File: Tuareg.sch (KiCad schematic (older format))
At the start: 1 part, among them CON1 ModICE_48

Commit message: changed to discrete crank vr sensor cirquitry
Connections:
- net con_vrspare+: no longer names the net of CON1.37 (D24)
- net con_vrspare-: no longer names the net of CON1.36 (D23)
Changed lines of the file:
@@
-$EndSheet
-$Sheet
-S 4300 6600 1800 950
-U 5BCA424F
-F0 "engine position sensors" 50
-F1 "engine_pos.sch" 50
-F2 "crank_signal" O R 6100 6800 50
-F3 "vr_spare" O R 6100 7150 50
-F4 "vr_crank+" I L 4300 6800 50
-F5 "vr_crank-" I L 4300 6950 50
-F6 "vr_spare-" I L 4300 7350 50
-F7 "vr_spare+" I L 4300 7150 50
 $EndSheet
 $Sheet
@@
 ach8
 Wire Wire Line
-	6100 7150 7450 7150
-Text Label 6400 7150 0    50   ~ 0
-vr_spare
-Wire Wire Line
 	6100 5400 7450 5400
 Wire Wire Line
@@
 	3450 6950 4300 6950
 Wire Wire Line
-	3450 7150 4300 7150
-Wire Wire Line
-	3450 7350 4300 7350
-Wire Wire Line
 	3450 7950 4300 7950
 Wire Wire Line
@@
 Text Label 3450 6950 0    50   ~ 0
 con_vrcrank-
-Text Label 3450 7150 0    50   ~ 0
-con_vrspare+
-Text Label 3450 7350 0    50   ~ 0
-con_vrspare-
 Text Label 3450 7950 0    50   ~ 0
 con_knock1
@@
 	20150 6650 20400 6650
 Wire Wire Line
-	20150 7150 20400 7150
-Wire Wire Line
 	20150 7250 20400 7250
 Text Label 20400 7750 0    50   ~ 0
@@
 Wire Wire Line
 	20400 7750 20150 7750
-Text Label 20400 7150 0    50   ~ 0
-con_vrspare+
-Text Label 20400 7050 0    50   ~ 0
-con_vrspare-
 Text Label 20400 6850 0    50   ~ 0
 con_vrcrank-
@@
 Wire Wire Line
 	20400 6850 20150 6850
-Wire Wire Line
-	20400 7050 20150 7050
 Wire Wire Line
 	20400 7350 20150 7350
@@
 Wire Wire Line
 	3450 4750 4300 4750
+$Sheet
+S 4300 6600 1800 950
+U 5BCA424F
+F0 "engine position sensors" 50
+F1 "engine_pos.sch" 50
+F2 "crank_signal" O R 6100 6800 50
+F3 "vr_crank+" I L 4300 6800 50
+F4 "vr_crank-" I L 4300 6950 50
+$EndSheet
 $EndSCHEMATC

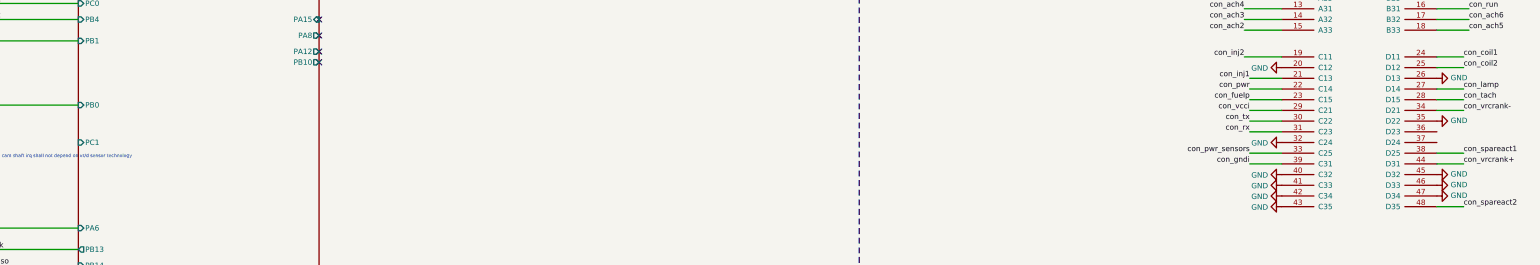
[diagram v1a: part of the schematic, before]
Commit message: migration to kicad 5.1.2
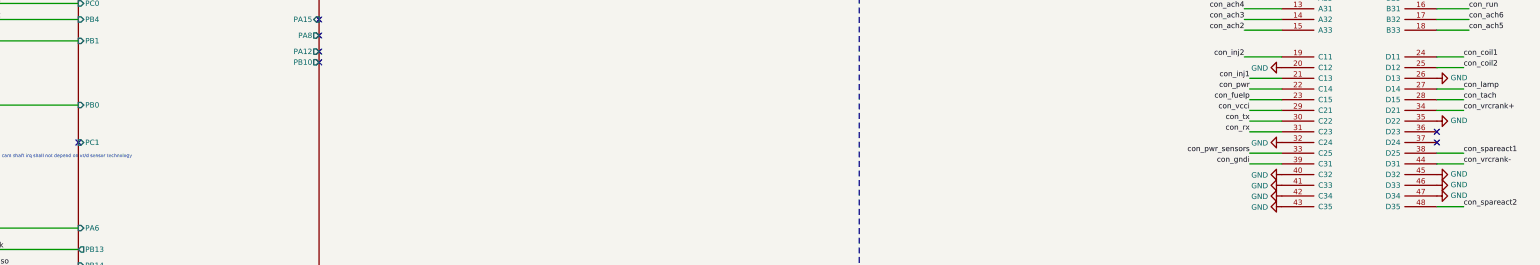
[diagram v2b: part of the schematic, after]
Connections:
- net con_vrcrank+: now also CON1.34 (D21); no longer CON1.44 (D31)
- net con_vrcrank-: now also CON1.44 (D31); no longer CON1.34 (D21)
- no-connect marks 4 -> 7
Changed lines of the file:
@@
 EESchema Schematic File Version 4
-LIBS:Tuareg-cache
-EELAYER 26 0
+EELAYER 29 0
 EELAYER END
 $Descr A2 23386 16535
@@
 Wire Wire Line
 	20400 7750 20150 7750
+Text Label 20400 7350 0    50   ~ 0
+con_vrcrank-
 Text Label 20400 6850 0    50   ~ 0
-con_vrcrank-
-Text Label 20400 7350 0    50   ~ 0
 con_vrcrank+
-Wire Wire Line
-	20400 6850 20150 6850
-Wire Wire Line
-	20400 7350 20150 7350
 $Comp
 L power:GND #PWR0103
@@
 F4 "vr_crank-" I L 4300 6950 50
 $EndSheet
+NoConn ~ 20150 7150
+NoConn ~ 20150 7050
+NoConn ~ 7450 7150
+Wire Wire Line
+	20400 7350 20150 7350
+Wire Wire Line
+	20400 6850 20150 6850
 $EndSCHEMATC

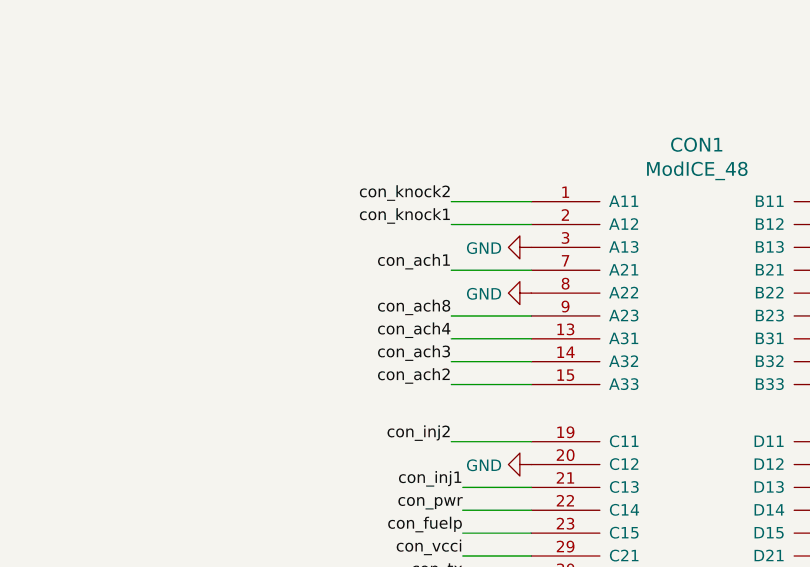
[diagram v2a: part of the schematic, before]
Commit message: minor design improvements for first series production
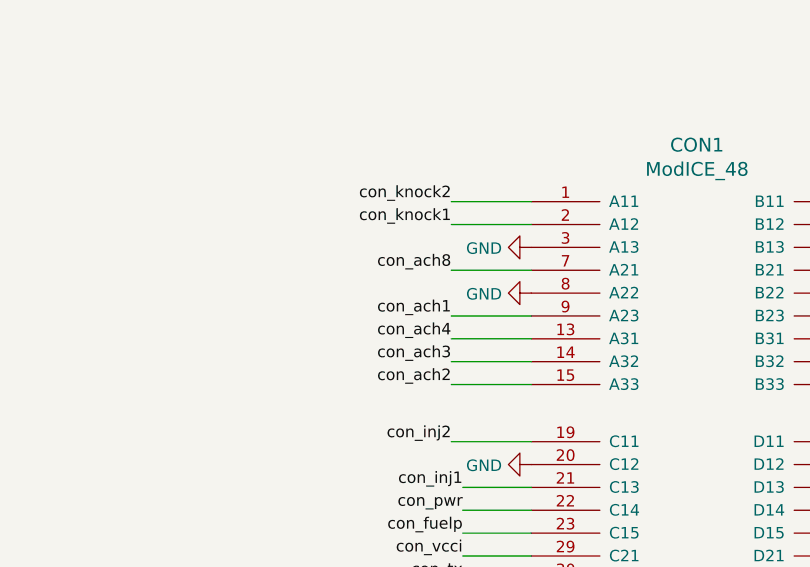
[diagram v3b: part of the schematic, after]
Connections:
- net con_ach1: now also CON1.9 (A23); no longer CON1.7 (A21)
- net con_ach8: now also CON1.7 (A21); no longer CON1.9 (A23)
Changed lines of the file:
@@
 EESchema Schematic File Version 4
+LIBS:Tuareg-cache
 EELAYER 29 0
 EELAYER END
@@
 Wire Wire Line
 	18700 6000 18350 6000
-Wire Wire Line
-	18350 5800 18700 5800
+Text Label 18350 5800 2    50   ~ 0
+con_ach1
 Text Label 18350 5600 2    50   ~ 0
-con_ach1
-Wire Wire Line
-	18350 5600 18700 5600
-Text Label 18350 5800 2    50   ~ 0
 con_ach8
 Text Label 20450 6000 0    50   ~ 0
@@
 Wire Wire Line
 	20400 6850 20150 6850
+Wire Wire Line
+	18350 5600 18700 5600
+Wire Wire Line
+	18350 5800 18700 5800
 $EndSCHEMATC

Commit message: cleaning up
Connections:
- net GND: now also CON1.36 (D23), CON1.37 (D24)
- no-connect marks 7 -> 5
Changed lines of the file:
@@
 F4 "vr_crank-" I L 4300 6950 50
 $EndSheet
-NoConn ~ 20150 7150
-NoConn ~ 20150 7050
 NoConn ~ 7450 7150
 Wire Wire Line
@@
 Wire Wire Line
 	18350 5800 18700 5800
+$Comp
+L power:GND #PWR?
+U 1 1 5D33E46F
+P 20150 7050
+F 0 "#PWR?" H 20150 6800 50  0001 C CNN
+F 1 "GND" V 20155 6922 50  0000 R CNN
+F 2 "" H 20150 7050 50  0001 C CNN
+F 3 "" H 20150 7050 50  0001 C CNN
+	1    20150 7050
+	0    -1   -1   0
+$EndComp
+$Comp
+L power:GND #PWR?
+U 1 1 5D33E6A9
+P 20150 7150
+F 0 "#PWR?" H 20150 6900 50  0001 C CNN
+F 1 "GND" V 20155 7022 50  0000 R CNN
+F 2 "" H 20150 7150 50  0001 C CNN
+F 3 "" H 20150 7150 50  0001 C CNN
+	1    20150 7150
+	0    -1   -1   0
+$EndComp
 $EndSCHEMATC

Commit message: cleaning up
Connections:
- net con_vrcrank- is gone; now on net con_vrcrank+: CON1.44 (D31)
- net GND: now also CON1.13 (A31), CON1.34 (D21), CON1.48 (D35); no longer CON1.37 (D24), CON1.8 (A22)
- net con_ach4: now also CON1.8 (A22); no longer CON1.13 (A31)
- net con_spareact2: now also CON1.37 (D24); no longer CON1.48 (D35)
- net con_vrcrank+: no longer CON1.34 (D21)
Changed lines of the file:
@@
 Wire Wire Line
 	20150 7250 20400 7250
-Text Label 20400 7750 0    50   ~ 0
+Text Label 20400 7150 0    50   ~ 0
 con_spareact2
 Text Label 20400 7250 0    50   ~ 0
 con_spareact1
-Wire Wire Line
-	20400 7750 20150 7750
+Text Label 20850 6850 0    50   ~ 0
+con_vrcrank-
 Text Label 20400 7350 0    50   ~ 0
-con_vrcrank-
-Text Label 20400 6850 0    50   ~ 0
 con_vrcrank+
 $Comp
@@
 Wire Wire Line
 	18700 7050 18400 7050
-Text Label 18350 5900 2    50   ~ 0
+Text Label 18350 5700 2    50   ~ 0
 con_ach4
 $Comp
 L power:GND #PWR0104
 U 1 1 5BF7B359
-P 18700 5700
-F 0 "#PWR0104" H 18700 5450 50  0001 C CNN
-F 1 "GND" V 18705 5572 50  0000 R CNN
-F 2 "" H 18700 5700 50  0001 C CNN
-F 3 "" H 18700 5700 50  0001 C CNN
-	1    18700 5700
-	0    1    1    0
-$EndComp
-Wire Wire Line
-	18350 5900 18700 5900
+P 18700 5900
+F 0 "#PWR0104" H 18700 5650 50  0001 C CNN
+F 1 "GND" V 18705 5772 50  0000 R CNN
+F 2 "" H 18700 5900 50  0001 C CNN
+F 3 "" H 18700 5900 50  0001 C CNN
+	1    18700 5900
+	0    1    1    0
+$EndComp
 Text Label 18350 6000 2    50   ~ 0
 con_ach3
@@
 NoConn ~ 7450 7150
 Wire Wire Line
-	20400 7350 20150 7350
-Wire Wire Line
-	20400 6850 20150 6850
-Wire Wire Line
 	18350 5600 18700 5600
 Wire Wire Line
 	18350 5800 18700 5800
 $Comp
-L power:GND #PWR?
+L power:GND #PWR0114
 U 1 1 5D33E46F
 P 20150 7050
-F 0 "#PWR?" H 20150 6800 50  0001 C CNN
+F 0 "#PWR0114" H 20150 6800 50  0001 C CNN
 F 1 "GND" V 20155 6922 50  0000 R CNN
 F 2 "" H 20150 7050 50  0001 C CNN
@@
 $EndComp
 $Comp
-L power:GND #PWR?
+L power:GND #PWR0115
 U 1 1 5D33E6A9
-P 20150 7150
-F 0 "#PWR?" H 20150 6900 50  0001 C CNN
-F 1 "GND" V 20155 7022 50  0000 R CNN
-F 2 "" H 20150 7150 50  0001 C CNN
-F 3 "" H 20150 7150 50  0001 C CNN
-	1    20150 7150
-	0    -1   -1   0
-$EndComp
+P 20150 7750
+F 0 "#PWR0115" H 20150 7500 50  0001 C CNN
+F 1 "GND" V 20155 7622 50  0000 R CNN
+F 2 "" H 20150 7750 50  0001 C CNN
+F 3 "" H 20150 7750 50  0001 C CNN
+	1    20150 7750
+	0    -1   -1   0
+$EndComp
+Wire Wire Line
+	18350 5700 18700 5700
+Wire Wire Line
+	20400 7350 20150 7350
+$Comp
+L power:GND #PWR0116
+U 1 1 5D5B1D42
+P 20600 6850
+F 0 "#PWR0116" H 20600 6600 50  0001 C CNN
+F 1 "GND" V 20605 6722 50  0000 R CNN
+F 2 "" H 20600 6850 50  0001 C CNN
+F 3 "" H 20600 6850 50  0001 C CNN
+	1    20600 6850
+	1    0    0    -1
+$EndComp
+Wire Wire Line
+	20850 6850 20600 6850
+Wire Wire Line
+	20600 6850 20150 6850
+Connection ~ 20600 6850
+Wire Wire Line
+	20400 7150 20150 7150
 $EndSCHEMATC

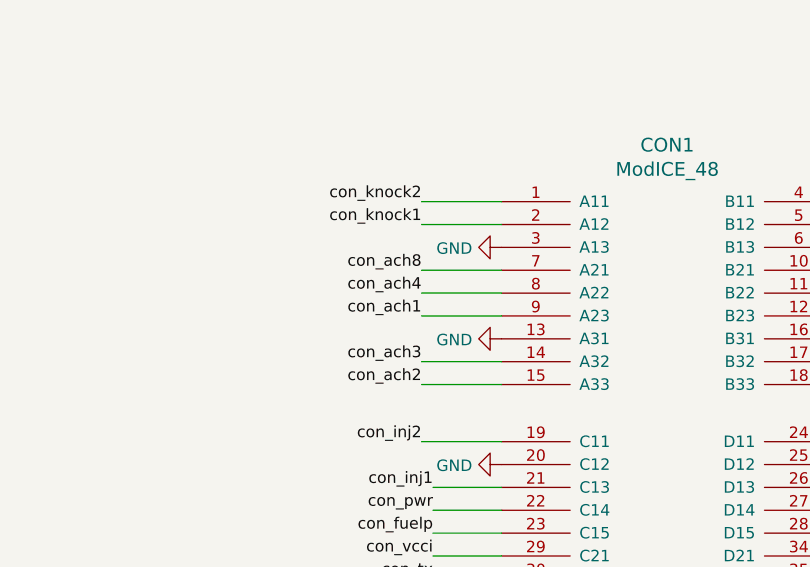
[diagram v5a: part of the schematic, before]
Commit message: added test points and cleaning up silk screen
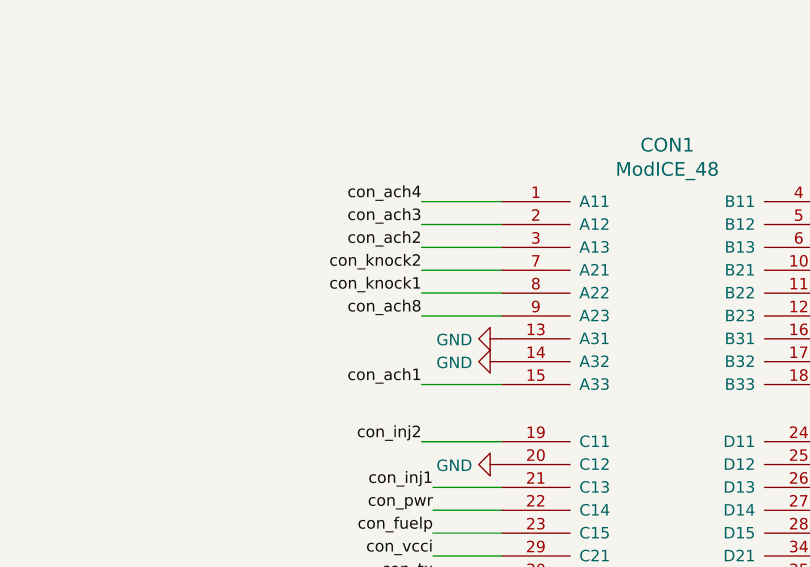
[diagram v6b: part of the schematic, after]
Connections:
- net GND: now also CON1.14 (A32); no longer CON1.3 (A13)
- net con_ach1: now also CON1.15 (A33); no longer CON1.9 (A23)
- net con_ach2: now also CON1.3 (A13); no longer CON1.15 (A33)
- net con_ach3: now also CON1.2 (A12); no longer CON1.14 (A32)
- net con_ach4: now also CON1.1 (A11); no longer CON1.8 (A22)
- net con_ach8: now also CON1.9 (A23); no longer CON1.7 (A21)
- net con_knock1: now also CON1.8 (A22); no longer CON1.2 (A12)
- net con_knock2: now also CON1.7 (A21); no longer CON1.1 (A11)
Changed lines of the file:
@@
 Wire Wire Line
 	18700 7050 18400 7050
-Text Label 18350 5700 2    50   ~ 0
+Text Label 18350 5300 2    50   ~ 0
 con_ach4
 $Comp
@@
 	0    1    1    0
 $EndComp
-Text Label 18350 6000 2    50   ~ 0
+Text Label 18350 5400 2    50   ~ 0
 con_ach3
+Text Label 18350 5500 2    50   ~ 0
+con_ach2
+Wire Wire Line
+	18350 6100 18700 6100
 Text Label 18350 6100 2    50   ~ 0
-con_ach2
-Wire Wire Line
-	18350 6100 18700 6100
-Wire Wire Line
-	18700 6000 18350 6000
+con_ach1
 Text Label 18350 5800 2    50   ~ 0
-con_ach1
-Text Label 18350 5600 2    50   ~ 0
 con_ach8
 Text Label 20450 6000 0    50   ~ 0
@@
 Text Label 18400 7250 2    50   ~ 0
 con_pwr_sensors
-Text Label 18350 5400 2    50   ~ 0
+Text Label 18350 5700 2    50   ~ 0
 con_knock1
-Text Label 18350 5300 2    50   ~ 0
+Text Label 18350 5600 2    50   ~ 0
 con_knock2
 Wire Wire Line
@@
 L power:GND #PWR069
 U 1 1 5BFEA4FA
-P 18700 5500
-F 0 "#PWR069" H 18700 5250 50  0001 C CNN
-F 1 "GND" V 18705 5372 50  0000 R CNN
-F 2 "" H 18700 5500 50  0001 C CNN
-F 3 "" H 18700 5500 50  0001 C CNN
-	1    18700 5500
+P 18700 6000
+F 0 "#PWR069" H 18700 5750 50  0001 C CNN
+F 1 "GND" V 18705 5872 50  0000 R CNN
+F 2 "" H 18700 6000 50  0001 C CNN
+F 3 "" H 18700 6000 50  0001 C CNN
+	1    18700 6000
 	0    1    1    0
 $EndComp
@@
 $EndComp
 Wire Wire Line
-	18350 5700 18700 5700
-Wire Wire Line
 	20400 7350 20150 7350
 $Comp
@@
 Wire Wire Line
 	20400 7150 20150 7150
+Wire Wire Line
+	18350 5500 18700 5500
+Wire Wire Line
+	18350 5700 18700 5700
 $EndSCHEMATC

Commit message: cleaned BOMs
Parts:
- CON1: Mouser (none) -> 538-581-01-48-009
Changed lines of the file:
@@
 F 2 "boctok_footprints:modICE_48" H 18850 7250 50  0001 C CNN
 F 3 "" H 19400 6200 50  0001 C CNN
+F 4 "538-581-01-48-009" H 19400 6200 50  0001 C CNN "Mouser"
 	1    19400 6200
 	1    0    0    -1
